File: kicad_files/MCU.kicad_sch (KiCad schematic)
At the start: 25 parts, among them J1 Conn_01x01_Socket, J2 Conn_01x01_Socket, J3 Conn_01x01_Socket, SW1 BOOT BUTTON, SW2 SW_Push, U1 STM32F407VGTx, Y1 8MHz Crystal

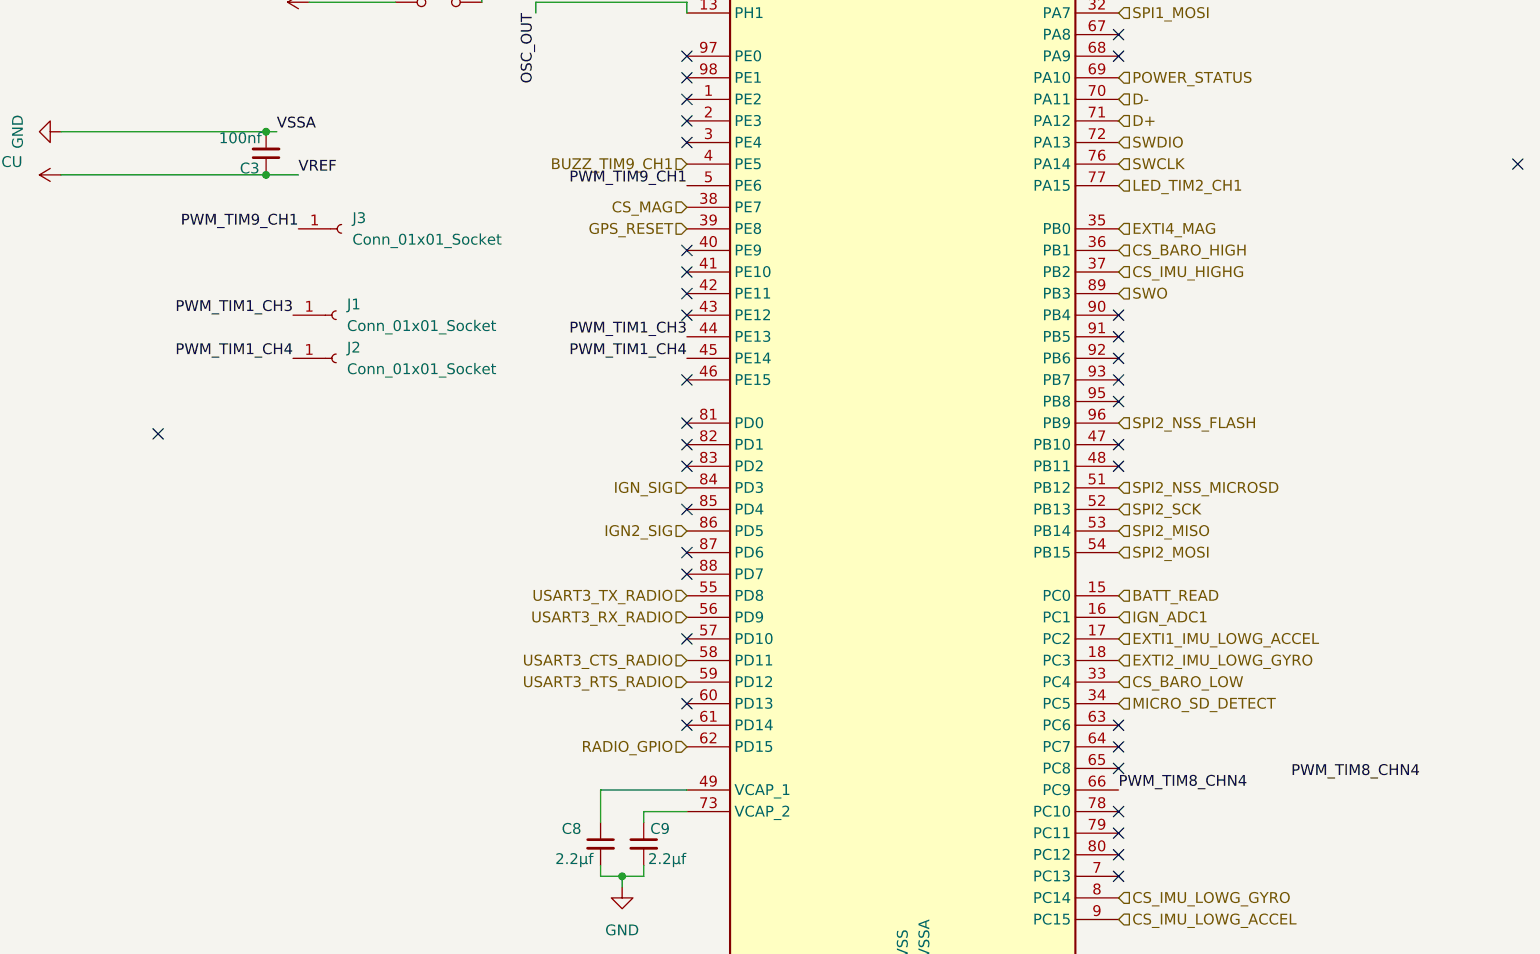
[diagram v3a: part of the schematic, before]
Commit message: fix buzzer
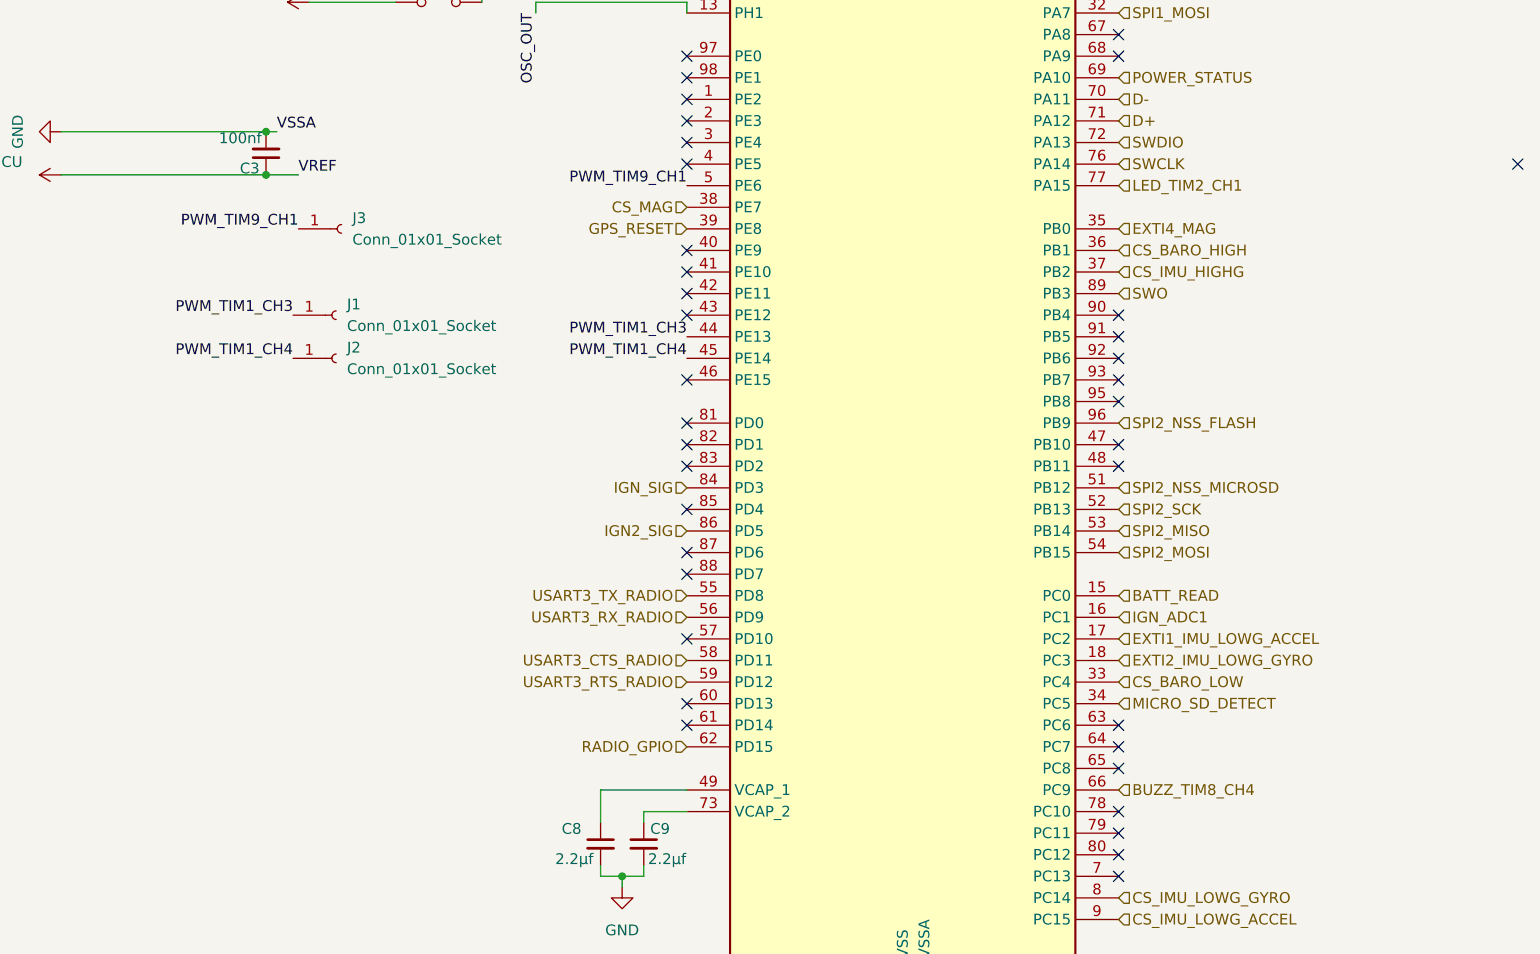
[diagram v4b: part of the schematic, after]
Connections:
- net BUZZ_TIM9_CH1: no longer names the net of U1.4 (PE5)
- net PWM_TIM8_CHN4 renamed BUZZ_TIM8_CH4
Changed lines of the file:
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@@
+	)
+	(no_connect
+		(at 199.39 129.54)
 	)
 	(no_connect
@@
 	(no_connect
 		(at 297.18 129.54)
-	)
-	(no_connect
-		(at 137.16 161.29)
 	)
 	(no_connect
@@
 		)
 	)
-	(label "PWM_TIM8_CHN4"
-		(at 250.19 203.2 0)
-		(effects
-			(font
-				(size 1.27 1.27)
-			)
-			(justify left bottom)
-		)
-	)
 	(label "VSSA"
 		(at 240.03 81.28 270)
@@
 		)
 	)
-	(label "PWM_TIM8_CHN4"
-		(at 270.51 201.93 0)
-		(effects
-			(font
-				(size 1.27 1.27)
-			)
-			(justify left bottom)
-		)
-	)
 	(label "PWM_TIM9_CH1"
 		(at 153.67 137.16 180)
@@
 		)
 	)
-	(hierarchical_label "BUZZ_TIM9_CH1"
-		(shape input)
-		(at 199.39 129.54 180)
-		(effects
-			(font
-				(size 1.27 1.27)
-			)
-			(justify right)
-		)
-	)
+	(hierarchical_label "BUZZ_TIM8_CH4"
+		(shape input)
+		(at 250.19 203.2 0)
+		(effects
+			(font
+				(size 1.27 1.27)
+			)
+			(justify left)
+		)
+	)

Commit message: Adjust naming
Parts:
- renumbered SW1 to BOOT1, SW2 to NRST1
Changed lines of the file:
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@@
 		(dnp no)
 		(fields_autoplaced yes)
-		(property "Reference" "SW2"
+		(property "Reference" "NRST1"
 			(at 184.15 87.6299 90)
 			(show_name no)
@@
 			(project "versorlite"
 				(path "/1a230af0-0a74-48f7-8607-b087121dda49/a6e36be3-aff5-4566-a903-d81edfd88a96"
-					(reference "SW2")
+					(reference "NRST1")
 					(unit 1)
 				)
@@
 		(dnp no)
 		(fields_autoplaced yes)
-		(property "Reference" "SW1"
+		(property "Reference" "BOOT1"
 			(at 170.18 102.87 0)
 			(show_name no)
@@
 			(project "versorlite"
 				(path "/1a230af0-0a74-48f7-8607-b087121dda49/a6e36be3-aff5-4566-a903-d81edfd88a96"
-					(reference "SW1")
-					(unit 1)
-				)
+					(reference "BOOT1")
+					(unit 1)
+				)
